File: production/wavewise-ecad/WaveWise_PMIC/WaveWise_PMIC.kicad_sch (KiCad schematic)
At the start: 0 parts

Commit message: power stuff
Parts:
- added R25, R26: 0, Resistor_SMD:R_0805_2012Metric, symbol Device:R
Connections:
- new net Connectors/SICO_PUMP_CONTROL: R25.2
- new net PICO (BICO)/BICO_PUMP_CTRL: R26.1
- new net PUMP_CONTROL: R25.1, R26.2
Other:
- sheet Connectors ports: added SICO_PUMP_CONTROL; removed none
- sheet PICO (BICO) ports: added BICO_PUMP_CTRL; removed PUMP_CTRL

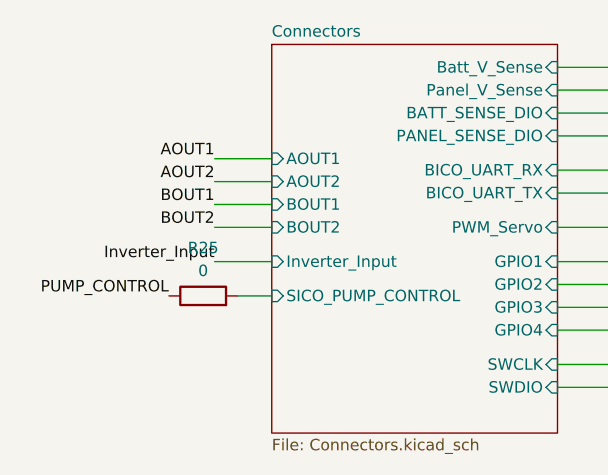
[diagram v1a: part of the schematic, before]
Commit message: add silkscreen
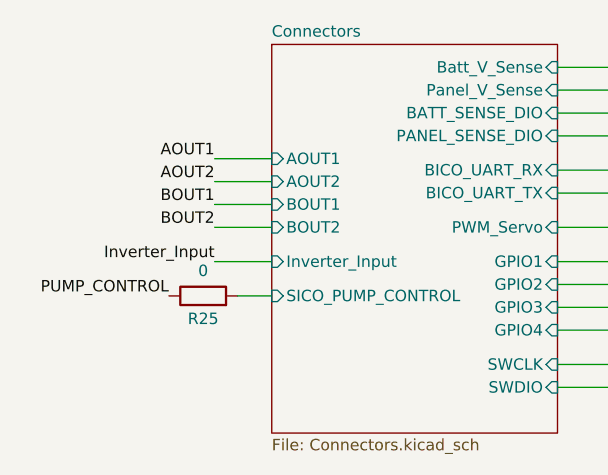
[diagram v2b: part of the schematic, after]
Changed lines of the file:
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@@
   )
   (symbol (lib_id "Device:R") (at 59.69 90.17 90) (unit 1)
-    (in_bom yes) (on_board yes) (dnp no) (fields_autoplaced)
-    (property "Reference" "R25" (at 59.69 84.836 90)
+    (in_bom yes) (on_board yes) (dnp no)
+    (property "Reference" "R25" (at 59.69 92.71 90)
       (effects (font (size 1.27 1.27)))
     )

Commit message: change pins on pico for layout
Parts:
- R26: footprint Resistor_SMD:R_0805_2012Metric -> Resistor_SMD:R_0805_2012Metric_Pad1.20x1.40mm_HandSolder
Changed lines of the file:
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@@
       (effects (font (size 1.27 1.27)))
     )
-    (property "Footprint" "Resistor_SMD:R_0805_2012Metric" (at 168.91 67.818 90)
+    (property "Footprint" "Resistor_SMD:R_0805_2012Metric_Pad1.20x1.40mm_HandSolder" (at 168.91 67.818 90)
       (effects (font (size 1.27 1.27)) hide)
     )
